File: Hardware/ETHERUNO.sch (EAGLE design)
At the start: 98 parts, among them IC1 MC33269DT-5.0, IC2 CP2102N-A01-GQFN24, IC4 LM358D, IC5 ATMEGA328P TQFP32, IC6 W6100-LQFP, IC7 MCP24AA025E48, J1 DC_2_1MM, J2 USB-C-16P-16P, P2 ICSP:MAIN, P4 microSD, Q1 FDN340P, Q2 2N7002, U1 HY931147C-RJ45

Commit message: Final routing and DRC for v4.0 release
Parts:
- removed L3: 0805 INDUCTOR, SuperHouse-DiscreteSemi:INDUCTOR0805-LARGE
- removed SJ1: GROUND, SuperHouse-Jumpers:SJC-NORMAL
- removed SJ2: UBOOT, SuperHouse-Jumpers:SJ-NORMAL
- SJ4: value (none) -> MODE
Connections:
- removed net N$328: LED4.C, RN1C.2
- removed net N$9: J2.GND, L3.1, R1.1, R2.1, Z1.2, Z2.2
- removed net USBGND: L3.2, SJ1.1
- new net N$8: LED4.C, RN1A.2
- net COLLED: now also RN1A.1; no longer RN1C.1
- net DTR: no longer SJ2.2
- net GND: now also J2.GND, R1.1, R2.1, Z1.2, Z2.2; no longer SJ1.2, SJ2.1
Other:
- note added: "3.3V 800mA Power Supply"
- note added: "DC / USB Auto Selection"
- note added: "EtherUNO (Arduino compatible with Ethernet)"
- note added: "Ethernet Status"
- note added: "MicroSD Card Slot"
- note added: "V4.0 (2020-07-12)"
- note added: "Wiznet Mode"
- note removed: "3V3 800mA Power Supply"
- note removed: "DCInput/USBVCC Auto-switch"
- note removed: "EtherUno (Arduino compatible with Ethernet)"
- note removed: "Micro SD Card Slot"
- note removed: "Status Display"
- note removed: "V4.0 (2020-05-15)"
- note removed: "Wiznet Mode Selection"
- moved on the sheet: A6, A7, C15, C16, C19, C20, C21, C22, C23, C24, C27, C29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

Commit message: Major rework for W5500, ready for v1.0 release
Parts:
- removed C30, C31: 100nF, SuperHouse-DiscreteSemi:CAP0603
- removed H1: Digital_8_13, SuperHouse-Connectors:M10-SOCKET
- removed H2: Power, SuperHouse-Connectors:M08-SOCKET
- removed IC7: MCP24AA025E48, freetronics-jon:MCP24AA025E48
- removed JP3: FT-POE-MODULE3, freetronics-master-v1.1:FT-POE-MODULE3
- removed L2, L4: 1uH 250mA 0805, SuperHouse-DiscreteSemi:INDUCTOR0805-LARGE
- removed LED10: D13/RED, SuperHouse-LEDs:LED0603
- removed LED9: YELLOW, SuperHouse-LEDs:LED0603
- removed P2: ICSP:MAIN, SuperHouse-Connectors:ICSP-PIN
- removed R12: 22.1K, SuperHouse-DiscreteSemi:RESISTOR0603
- removed R13: 47.5K, SuperHouse-DiscreteSemi:RESISTOR0603
- removed R14, R15: 4K7, SuperHouse-DiscreteSemi:RESISTOR0603
- removed RN8: 2K2, SuperHouse-DiscreteSemi:4R-NCAY16
- removed SJ5, SJ6, SJ7: SJC, SuperHouse-Jumpers:SJC-NORMAL
- removed U$17, U$19: CRYSTAL-GND3X2, SuperHouse-Oscillators:CRYSTAL-GND3X2
- added C11: 1uF 0603, SuperHouse-DiscreteSemi:CAP0603
- added C12: 100nF 0603, SuperHouse-DiscreteSemi:CAP0603
- added C2, C8: 22pF 0603, SuperHouse-DiscreteSemi:CAP0603
- added IC3: ATMEGA328P TQFP32, SuperHouse-MCUs:AVR-MEGA8-AI
- added J10: ICSP:USB, SuperHouse-Connectors:ICSP-PIN
- added J5: DC_2_1MM, SuperHouse-Connectors:POWER_JACK-SLOTS
- added J6: USB-C-16P-16P, SuperHouse-Connectors:USB-C-16P-16P
- added J7: INT, SuperHouse-Connectors:M01-PLAIN
- added J8: FT-POE-MODULE3, freetronics-master-v1.1:FT-POE-MODULE3
- added J9: ICSP:MAIN, SuperHouse-Connectors:ICSP-PIN
- added LED1: PWR/BLUE, SuperHouse-LEDs:LED0603
- added R10: 12.4K 1%, SuperHouse-DiscreteSemi:RESISTOR0603
- added R11: 1M, SuperHouse-DiscreteSemi:RESISTOR0603
- added R4, R5: 4K7, SuperHouse-DiscreteSemi:RESISTOR0603
- added RN7: 2K2, SuperHouse-DiscreteSemi:4R-NCAY16
- added SJ1: RESET-EN, SuperHouse-Jumpers:SJC-NORMAL
- added SJ2: UBOOT, SuperHouse-Jumpers:SJ-NORMAL
- added XTL1, XTL2: 16MHz, SuperHouse-Oscillators:CRYSTAL-GND3X2
- added XTL3: 25MHz, SuperHouse-Oscillators:CRYSTAL-GND3X2
- A6: value M01 -> A6
- A7: value M01 -> A7
- C14, C29: value 100nF 0603 -> 100nF
- C15: value 13pF -> 10nF
- C16: value 13pF -> 4.7uF
- C18: value 100nF -> 10nF
- C20, C21: value 22pF 0603 -> 15pF
- C3, C4: value 10uF 6.3V A TANT -> 18pF; device SuperHouse-DiscreteSemi:CAP_POL1206 -> SuperHouse-DiscreteSemi:CAP0603
- C5, C6: device SuperHouse-DiscreteSemi:CAP_POLD -> rcl:CPOL-EUD
- CD: value M01 -> M01-PLAIN
- IC2: value CP2102N-A01-GQFN24 -> ATMEGA16U2-MU; device SuperHouse-ICs:CP2104 -> SuperHouse-MCUs:ATMEGA8U2QFN
- IC4: device linear:LM358D -> SuperHouse-ICs:LM358D
- IC5: value ATMEGA328P TQFP32 -> W5500-LQFP; device SuperHouse-MCUs:ATMEGA8-AI -> SuperHouse-ICs:W5500-LQFP
- IC6: value W6100-LQFP -> MCP24AA025E48; device SuperHouse-ICs:W6100-LQFP -> freetronics-jon:MCP24AA025E48
- J1: value DC_2_1MM -> Digital_8_13; device SuperHouse-Connectors:POWER_JACK-SLOTS -> SuperHouse-Connectors:M10-SOCKET
- J2: value USB-C-16P-16P -> Power; device SuperHouse-Connectors:USB-C-16P-16P -> SuperHouse-Connectors:M08-SOCKET
- L1: device SuperHouse-DiscreteSemi:INDUCTOR0805-LARGE -> rcl:L-USL2012C
- LED2: value PWR/BLUE -> YELLOW
- LED3: value YELLOW -> TX/YEL
- LED4: value RED -> RX/GRN
- LED5: value TX/YEL -> GREEN
- LED6: value RX/GRN -> GREEN
- LED7: value GREEN -> YELLOW
- LED8: value GREEN -> D13/RED
- R1, R2: value 5K1 -> 22R
- R3: value 10K -> 1K
- R6: value 12K 1% -> 5K1
- R7: value 300R 1% -> 5K1
- R8: value 1K 0603 -> 10K
- RN1, RN2: value 330R -> 1K
- SJ3: value RESET-EN -> SJC-NORMAL
- SJ4: value MODE -> SJC-NORMAL; device SuperHouse-Jumpers:SJ-NORMAL -> SuperHouse-Jumpers:SJC-NORMAL
- VR1: value LD1117-SOT223 -> LD1117-SOT89; device SuperHouse-Regulators:LD1117-SOT223 -> SuperHouse-Regulators:LD1117-SOT89
- VR2: value LD1117-SOT89 -> LD1117-SOT223; device SuperHouse-Regulators:LD1117-SOT89 -> SuperHouse-Regulators:LD1117-SOT223
- renumbered H3 to J3, H4 to J4, P4 to J11
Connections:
- removed net 1V2A: C17.1, C4.+, IC6.1V2A, L1.2
- removed net 1V2D: C26.1, C28.1, C3.+, C30.1, C31.1, IC6.1V2D, L4.2
- removed net COLLED: IC6.!COL, RN1A.1
- removed net D+: IC2.D+, J2.D+, Z1.1
- removed net D-: IC2.D-, J2.D-, Z2.1
- removed net D11_MOSI: H1.4, IC5.PB3(MOSI/OC2), IC6.MOSI, P2.4, RN6C.2
- removed net D12_MISO: H1.5, IC5.PB4(MISO), IC6.MISO, J11.DO, P2.1
- removed net MODE: IC6.MOD0, R3.2, SJ4.1
- removed net N$32: C16.1, IC6.XSCI, U$17.XTL2
- removed net N$36: IC6.RSET_BG, R6.1
- removed net N$37: IC6.!INT, R9.1
- removed net N$39: IC2.VBUS, R12.1, R13.2
- removed net RX_LED: IC2.GPIO_1, RN3B.2
- removed net TX_LED: IC2.GPIO_0, RN3A.2
- new net CIPO2: IC2.(MISO)PB3, J10.1
- new net COPI2: IC2.(MOSI)PB2, J10.4
- new net D11_COPI: IC3.PB3(MOSI/OC2), IC5.COPI, J1.4, J9.4, RN6C.2
- new net D12_CIPO: IC3.PB4(MISO), IC5.CIPO, J1.5, J11.DO, J9.1
- new net N$113: C2.2, IC2.XTAL2, XTL1.1
- new net N$117: C11.1, IC2.UCAP
- new net N$16: J6.D+, R2.2, Z1.1
- new net N$17: J6.D-, R1.2, Z2.1
- new net N$31: C16.1, IC5.TOCAP
- new net N$33: IC5.EXRES1, R10.1
- new net N$9: J6.CC2, R6.2
- new net RD+: IC2.D+, R2.1
- new net RD-: IC2.D-, R1.1
- new net RESET2: IC2.RESET, J10.5, RN4A.1
- new net RXLED: IC2.PD4, RN3B.2
- new net SCK2: IC2.(SCLK)PB1, J10.3
- new net TXLED: IC2.(XCK)PD5, RN3A.2
- net 1V2O: now also C15.1, IC5.1V2O; no longer IC6.1V2O, L1.1, L4.1
- net 3.3V: now also C25.1, IC5.3V3D, J2.4, L1.1, LED2.A; no longer H2.4, IC2.REGIN, IC2.VDD, IC2.VIO, IC6.3V3D, L2.1, LED3.A, LED4.A, LED8.A, LED9.A, R9.2, SJ4.2
- net 3V3A: now also C17.1, C26.1, C28.1, IC5.3V3A, L1.2; no longer C25.1, IC6.3V3A, L2.2
- net 5V: now also C12.1, IC2.AVCC, IC2.VCC, IC3.AVCC, IC3.VCC@1, IC3.VCC@2, IC6.VCC, J10.2, J2.2, J2.5, J9.2, LED1.A, LED3.A, LED4.A, LED8.A, R4.1, R5.1, R8.2, RN4A.2; no longer H2.2, H2.5, IC5.AVCC, IC5.VCC@1, IC5.VCC@2, IC7.VCC, LED10.A, LED2.A, P2.2, R12.2, R14.1, R15.1
- net A0: now also IC3.PC0(ADC0); no longer IC5.PC0(ADC0)
- net A1: now also IC3.PC1(ADC1); no longer IC5.PC1(ADC1)
- net A2: now also IC3.PC2(ADC2); no longer IC5.PC2(ADC2)
- net A3: now also IC3.PC3(ADC3); no longer IC5.PC3(ADC3)
- net A4_SDA: now also IC3.PC4(ADC4/SDA), J1.9, SJ3.1; no longer H1.9, IC5.PC4(ADC4/SDA), SJ5.1
- net A5_SCL: now also IC3.PC5(ADC5/SCL), J1.10, SJ4.1; no longer H1.10, IC5.PC5(ADC5/SCL), SJ6.1
- net ACTLED: now also IC5.!ACT, RN2A.2; no longer IC6.!ACT
- net AREF: now also IC3.AREF, J1.8; no longer H1.8, IC5.AREF
- net D0_RX: now also IC3.PD0(RXD); no longer IC5.PD0(RXD)
- net D10_CS: now also IC3.PB2(SS/OC1B), IC5.!CS, J1.3; no longer H1.3, IC5.PB2(SS/OC1B), IC6.!CS
- net D13_SCK: now also IC3.PB5(SCK), IC5.SCLK, J1.6, J9.3; no longer H1.6, IC5.PB5(SCK), IC6.SCLK, P2.3
- net D1_TX: now also IC3.PD1(TXD); no longer IC5.PD1(TXD)
- net D2: now also IC3.PD2(INT0); no longer IC5.PD2(INT0)
- net D3: now also IC3.PD3(INT1); no longer IC5.PD3(INT1)
- net D4: now also IC3.PD4(XCK/T0), RN6D.2; no longer IC5.PD4(XCK/T0), SJ7.2
- net D5: now also IC3.PD5(T1); no longer IC5.PD5(T1)
- net D6: now also IC3.PD6(AIN0); no longer IC5.PD6(AIN0)
- net D7: now also IC3.PD7(AIN1); no longer IC5.PD7(AIN1)
- net D8: now also IC3.PB0(ICP), J1.1; no longer H1.1, IC5.PB0(ICP)
- net D9: now also IC3.PB1(OC1A), J1.2; no longer H1.2, IC5.PB1(OC1A)
- net DTR: now also IC2.(CTS)PD7, SJ1.1, SJ2.2; no longer IC2.DTR, SJ3.1
- net FDXLED: now also IC5.!DPX; no longer IC6.!DPX, RN2A.2
- net GND: now also C11.2, C12.2, C2.1, C3.2, C4.2, C8.1, IC2.PAD, IC2.UGND, IC3.AGND, IC3.GND@1, IC3.GND@2, IC5.GND, IC6.A0, IC6.A1, J1.7, J10.6, J2.6, J2.7, J5.GND, J5.GNDBREAK, J6.GND, J8.GND[1], J9.6, R10.2, R6.1, R7.1, R9.2, RN7A.1, RN7B.1, RN7C.1, SJ2.1, XTL1.GND, XTL2.GND, XTL3.GND; no longer C3.-, C30.2, C31.2, C4.-, H1.7, H2.6, H2.7, IC2.GND_PAD, IC5.GND@1, IC5.GND@2, IC6.GNDA, IC6.MOD1, IC6.MOD2, IC6.MOD3, IC7.A0, IC7.A1, IC7.GND, J1.GND, J1.GNDBREAK, J2.GND, JP3.GND[1], P2.6, R1.1, R13.1, R2.1, R3.1, R7.2, RN8A.1, RN8B.1, RN8C.1, U$17.GND, U$17.GND2, U$19.GND, U$19.GND2
- net LINKLED: now also IC5.!LINK; no longer IC6.!LINK
- net N$10: now also C4.1, IC5.XO, R11.1, XTL3.2; no longer J2.CC2, R1.2
- net N$11: now also LED4.C; no longer LED6.C
- net N$115: now also J6.VBUS; no longer J2.VBUS
- net N$13: now also LED3.C; no longer LED5.C
- net N$14: now also LED1.C; no longer LED2.C
- net N$2: now also IC3.PB6(XTAL1/TOSC1), XTL2.1; no longer IC5.PB6(XTAL1/TOSC1), U$19.XTL1
- net N$20: now also RN7A.2; no longer RN8A.2
- net N$21: now also IC3.ADC7; no longer IC5.ADC7
- net N$22: now also IC3.ADC6; no longer IC5.ADC6
- net N$24: now also RN7B.2; no longer RN8B.2
- net N$25: now also RN7C.2; no longer RN8C.2
- net N$26: now also LED6.C; no longer LED8.C
- net N$27: now also C3.1, IC5.XI/CLKIN, R11.2, XTL3.1; no longer RN6D.2, SJ7.1
- net N$28: now also LED7.C; no longer LED9.C
- net N$29: now also IC6.SDA, R4.2, SJ3.2; no longer IC7.SDA, R14.2, SJ5.2
- net N$3: now also SJ1.2; no longer SJ3.2
- net N$30: now also J6.CC1, R7.2; no longer C15.1, IC6.XSCO, U$17.XTL1
- net N$327: now also LED5.C; no longer LED7.C
- net N$329: now also LED2.C; no longer LED3.C
- net N$34: now also IC5.RSVD6, R9.1; no longer J2.CC1, R2.2
- net N$35: now also IC5.!INT, J7.1, R8.1; no longer R6.2, R7.1
- net N$4: now also LED8.C, R3.2; no longer LED10.C, R8.2
- net N$5: now also IC6.SCL, R5.2, SJ4.2; no longer IC7.SCL, R15.2, SJ6.2
- net N$6: now also R3.1; no longer R8.1
- net N$60: now also J5.PWR; no longer J1.PWR
- net N$68: now also J8.V+[3]; no longer JP3.V+[3]
- net N$69: now also J8.V-[2]; no longer JP3.V-[2]
- net N$7: now also IC3.PB7(XTAL2/TOSC2), XTL2.2; no longer IC5.PB7(XTAL2/TOSC2), U$19.XTL2
- net N$8: now also C8.2, IC2.XTAL1, XTL1.2; no longer LED4.C, RN1A.2
- net RESET: now also IC3.PC6(/RESET), IC5.!RESET, J2.3, J9.5; no longer H2.3, IC5.PC6(/RESET), IC6.!RESET, P2.5
- net RXIN: now also IC5.RXIN; no longer IC6.RXIN
- net RXIP: now also IC5.RXIP; no longer IC6.RXIP
- net SPDLED: now also IC5.!SPD; no longer IC6.!SPD
- net TXON: now also IC5.TXON; no longer IC6.TXON
- net TXOP: now also IC5.TXOP; no longer IC6.TXOP
- net USBRXD: now also IC2.(TXD1)PD3; no longer IC2.TXD
- net USBTXD: now also IC2.(RXD1)PD2; no longer IC2.RXD
- net USBVCC: now also IC2.UVCC
- net VIN: now also J2.8, J8.VIN[4]; no longer H2.8, JP3.VIN[4]
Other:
- note added: "3V3 800mA Power Supply"
- note added: "5V / 3.3V Decoupling"
- note added: "D2 used if Wiznet Ethernet IC "interrupt" jumper enabled."
- note added: "DCInput/USBVCC Auto-switch"
- note added: "EtherUNO (Arduino UNO compatible with Ethernet)"
- note added: "ICSP Headers"
- note added: "Mod0-2 pulled high internally. This enables all modes."
- note added: "Prototyping Area"
- note added: "SKU: ETHERUNO"
- note added: "V1.0 (2020-08-05)"
- note added: "Wiznet W5500 !INT is an output. The 10K pull-up is included so that if this output is connected to an Arduino pin, it will be biased HIGH and can be used to detect Ethernet activity when pulled LOW."
- note added: "Wiznet W5500 Ethernet Controller"
- note added: "micro SD Card Slot"
- note removed: "(Linked)"
- note removed: "1.2V / 3.3V Decoupling"
- note removed: "1V2O is generated by the Wiznet W6100"
- note removed: "3.3V 800mA Power Supply"
- note removed: "DC / USB Auto Selection"
- note removed: "EtherUNO (Arduino compatible with Ethernet)"
- note removed: "Ethernet Controller"
- note removed: "ICSP Header"
- note removed: "MicroSD Card Slot"
- note removed: "Open: W6100 (default) Closed: W5500"
- note removed: "SKU: EU"
- note removed: "To power source selection circuit"
- note removed: "V4.0 (2020-07-12)"
- note removed: "Wiznet Mode"

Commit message: Fix Ethernet data line bias resistors. Add strong pullups and pulldowns to mode and RSVD pins. Improve silkscreen. Add diode to PoE VIN to protect against backpower.
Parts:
- removed C22: 100nF, SuperHouse-DiscreteSemi:CAP0603
- added D2: 1N4004, SuperHouse-DiscreteSemi:DIODESMA
- added R12: 10R, SuperHouse-DiscreteSemi:RESISTOR0603
- added RN8, RN9: 10K, SuperHouse-DiscreteSemi:4R-NCAY16
- C23: value 100nF -> 10nF
- C24: value 100nF -> 22nF
- D1: value 1N4004 SMB -> 1N4004
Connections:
- removed net N$321: C23.1, RN5A.2, RN5B.2
- new net N$15: D2.A, J8.VIN[4]
- new net N$32: C24.1, R12.2, U1.TXCT
- new net N$36: IC5.MOD0, RN8A.1
- new net N$37: IC5.MOD1, RN8B.1
- new net N$38: IC5.MOD2, RN8C.1
- new net N$39: IC5.RSVD5, RN8D.1
- new net N$40: IC5.RSVD4, RN9A.1
- new net N$41: IC5.RSVD3, RN9B.1
- new net N$42: IC5.RSVD2, RN9C.1
- new net N$43: IC5.RSVD1, RN9D.1
- net 3.3V: now also R12.1, RN5C.2, RN5D.2, RN8A.2, RN8B.2, RN8C.2
- net 3V3A: no longer C22.1, U1.RXCT, U1.TXCT
- net GND: now also RN8D.2, RN9A.2, RN9B.2, RN9C.2, RN9D.2; no longer C22.2
- net N$1: now also C23.1, RN5A.2, RN5B.2, U1.RXCT; no longer C24.1, RN5C.2, RN5D.2
- net N$34: now also IC5.RSVD; no longer IC5.RSVD6
- net VIN: now also D2.C; no longer J8.VIN[4]
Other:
- note added: "Mod0-2 pulled high enables all modes. Strong external pullups improves EMC performance."
- note added: "V1.1 (2020-09-10)"
- note removed: "Mod0-2 pulled high internally. This enables all modes."
- note removed: "V1.0 (2020-08-05)"
- moved on the sheet: C16, C23, C24, C3, C4, J7, R10, R11, R8, R9, RN2A, RN2B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

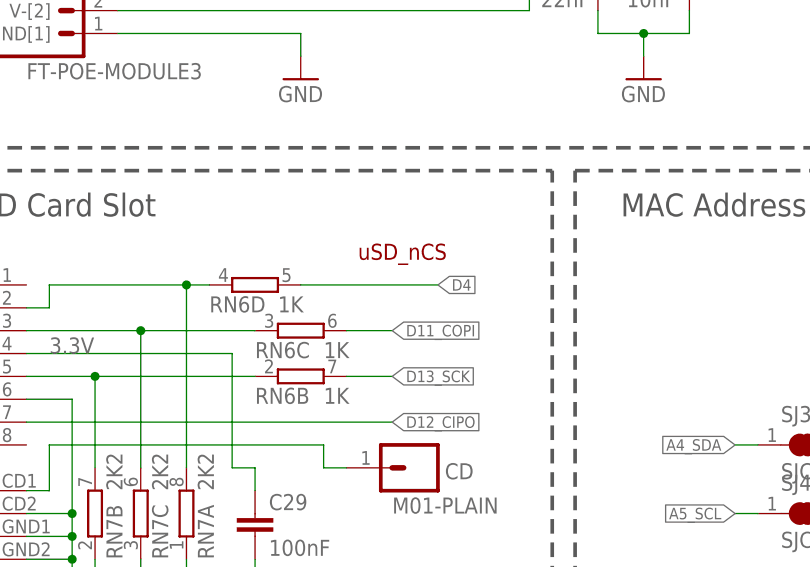
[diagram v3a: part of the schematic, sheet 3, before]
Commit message: Added cut-track jumper to isolate D4 from SD_CS
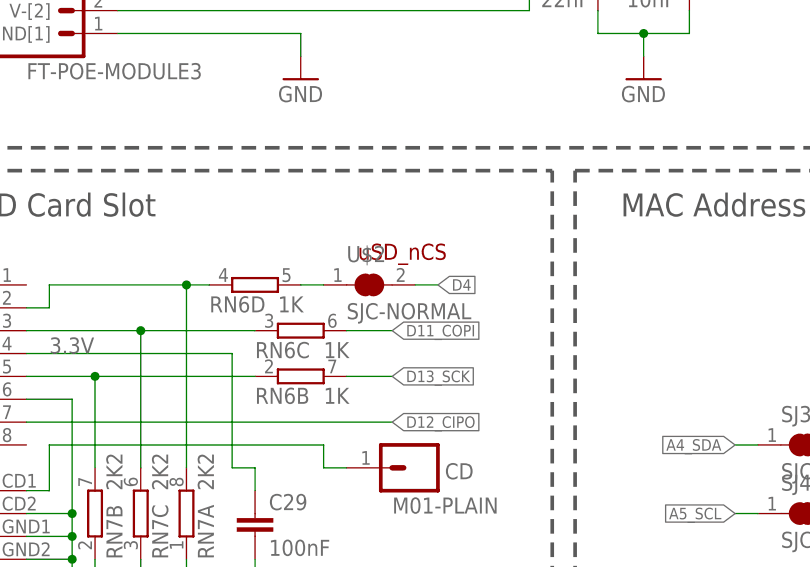
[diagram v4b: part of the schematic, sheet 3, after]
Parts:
- added U$2: SJC-NORMAL, SuperHouse-Jumpers:SJC-NORMAL
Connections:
- new net N$44: RN6D.2, U$2.1
- net D4: now also U$2.2; no longer RN6D.2
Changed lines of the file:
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@@
 <part name="GND12" library="SuperHouse-SupplySymbols" library_urn="urn:adsk.eagle:library:11790503" deviceset="GND" device=""/>
 <part name="RN9" library="SuperHouse-DiscreteSemi" library_urn="urn:adsk.eagle:library:11768461" deviceset="4R-N" device="CAY16" package3d_urn="urn:adsk.eagle:package:11872201/2" value="10K"/>
+<part name="U$2" library="SuperHouse-Jumpers" library_urn="urn:adsk.eagle:library:12190622" deviceset="SJC" device="-NORMAL" package3d_urn="urn:adsk.eagle:package:7066342/1"/>
 </parts>
 <sheets>
@@
 <attribute name="NAME" x="229.87" y="129.032" size="1.778" layer="95"/>
 </instance>
+<instance part="U$2" gate="G$1" x="66.04" y="66.04" smashed="yes">
+<attribute name="NAME" x="63.5" y="68.58" size="1.778" layer="95"/>
+<attribute name="VALUE" x="63.5" y="62.23" size="1.778" layer="96"/>
+</instance>
 </instances>
 <busses>
@@
 </segment>
 </net>
-<net name="D4" class="0">
-<segment>
-<wire x1="58.42" y1="66.04" x2="73.66" y2="66.04" width="0.1524" layer="91"/>
-<pinref part="RN6" gate="D" pin="2"/>
-<label x="73.66" y="66.04" size="1.27" layer="95" xref="yes"/>
-</segment>
-</net>
 <net name="3.3V" class="0">
 <segment>
@@
 </segment>
 </net>
+<net name="N$44" class="0">
+<segment>
+<pinref part="RN6" gate="D" pin="2"/>
+<pinref part="U$2" gate="G$1" pin="1"/>
+<wire x1="58.42" y1="66.04" x2="60.96" y2="66.04" width="0.1524" layer="91"/>
+</segment>
+</net>
+<net name="D4" class="0">
+<segment>
+<pinref part="U$2" gate="G$1" pin="2"/>
+<wire x1="71.12" y1="66.04" x2="73.66" y2="66.04" width="0.1524" layer="91"/>
+<label x="73.66" y="66.04" size="1.27" layer="95" xref="yes"/>
+</segment>
+</net>
